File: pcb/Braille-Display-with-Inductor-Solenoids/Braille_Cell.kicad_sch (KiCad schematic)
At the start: 43 parts, among them U2 AD116, U3 AD116, U4 AD116, U5 AD116, U6 AD116, U7 AD116

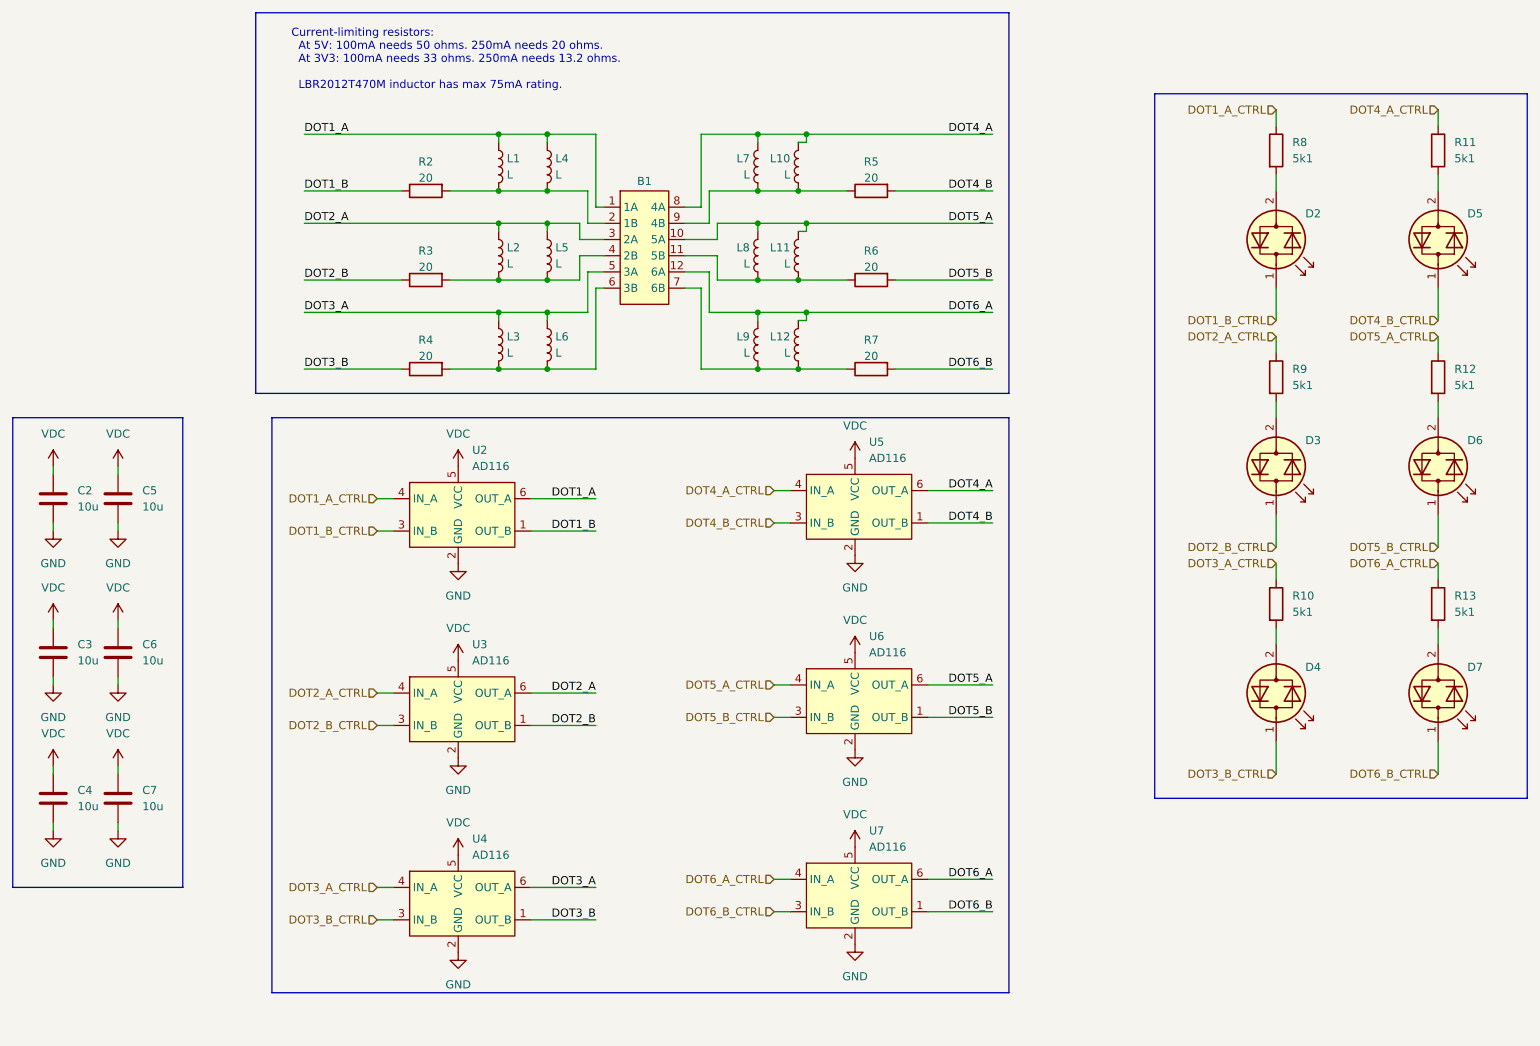
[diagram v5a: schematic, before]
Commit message: Update SMD solenoid with THT pads
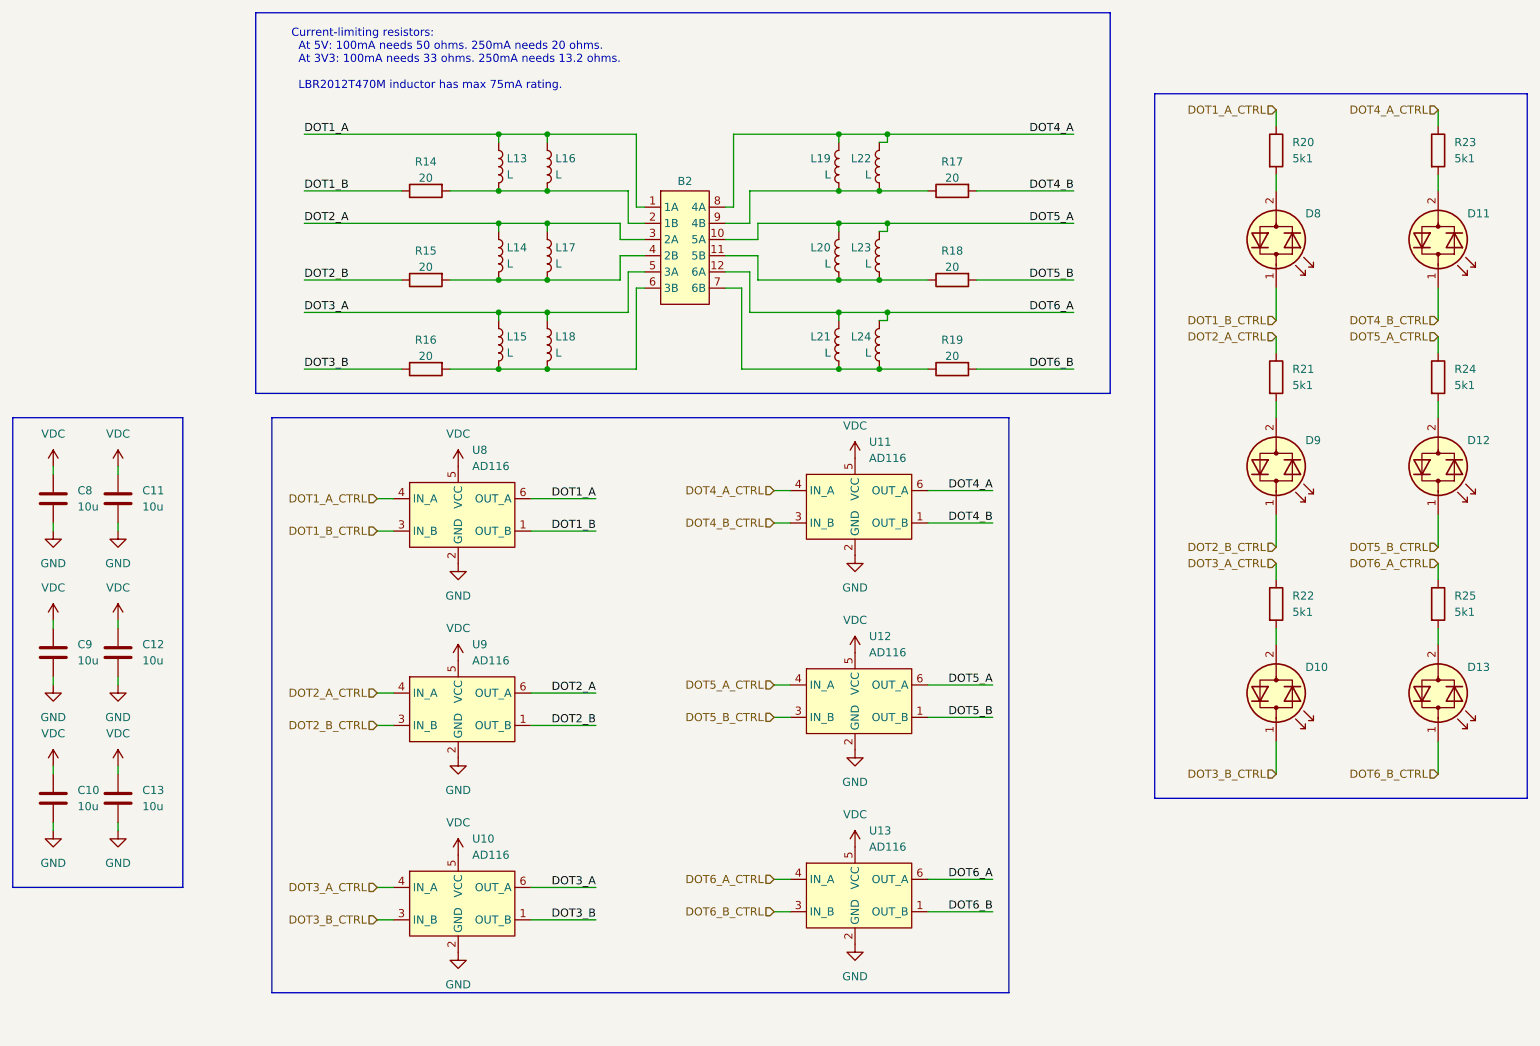
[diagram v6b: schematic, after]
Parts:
- renumbered B1 to B2, C4 to C10, C5 to C11, C6 to C12, C7 to C13, C2 to C8, C3 to C9, D4 to D10, D5 to D11, D6 to D12, D7 to D13, D2 to D8, D3 to D9, L1 to L13, L2 to L14, L3 to L15, L4 to L16, L5 to L17, L6 to L18, L7 to L19, L8 to L20, L9 to L21, L10 to L22, L11 to L23, L12 to L24, R2 to R14, R3 to R15, R4 to R16, R5 to R17, R6 to R18, R7 to R19, R8 to R20, R9 to R21, R10 to R22, R11 to R23, R12 to R24, R13 to R25, U4 to U10, U5 to U11, U6 to U12, U7 to U13, U2 to U8, U3 to U9
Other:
- moved on the sheet: B2, L19, L20, L21, L22, L23, L24, R17, R18, R19
